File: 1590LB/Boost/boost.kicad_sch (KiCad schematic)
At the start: 22 parts, among them Q201 MMBF5103, Q202 BC847C, Q203 BC857C, Q204 NMB2227A, Q205 DMMT5401, Q206 DMMT5551, Q207 DMMT5401, Q208 DMMT5401

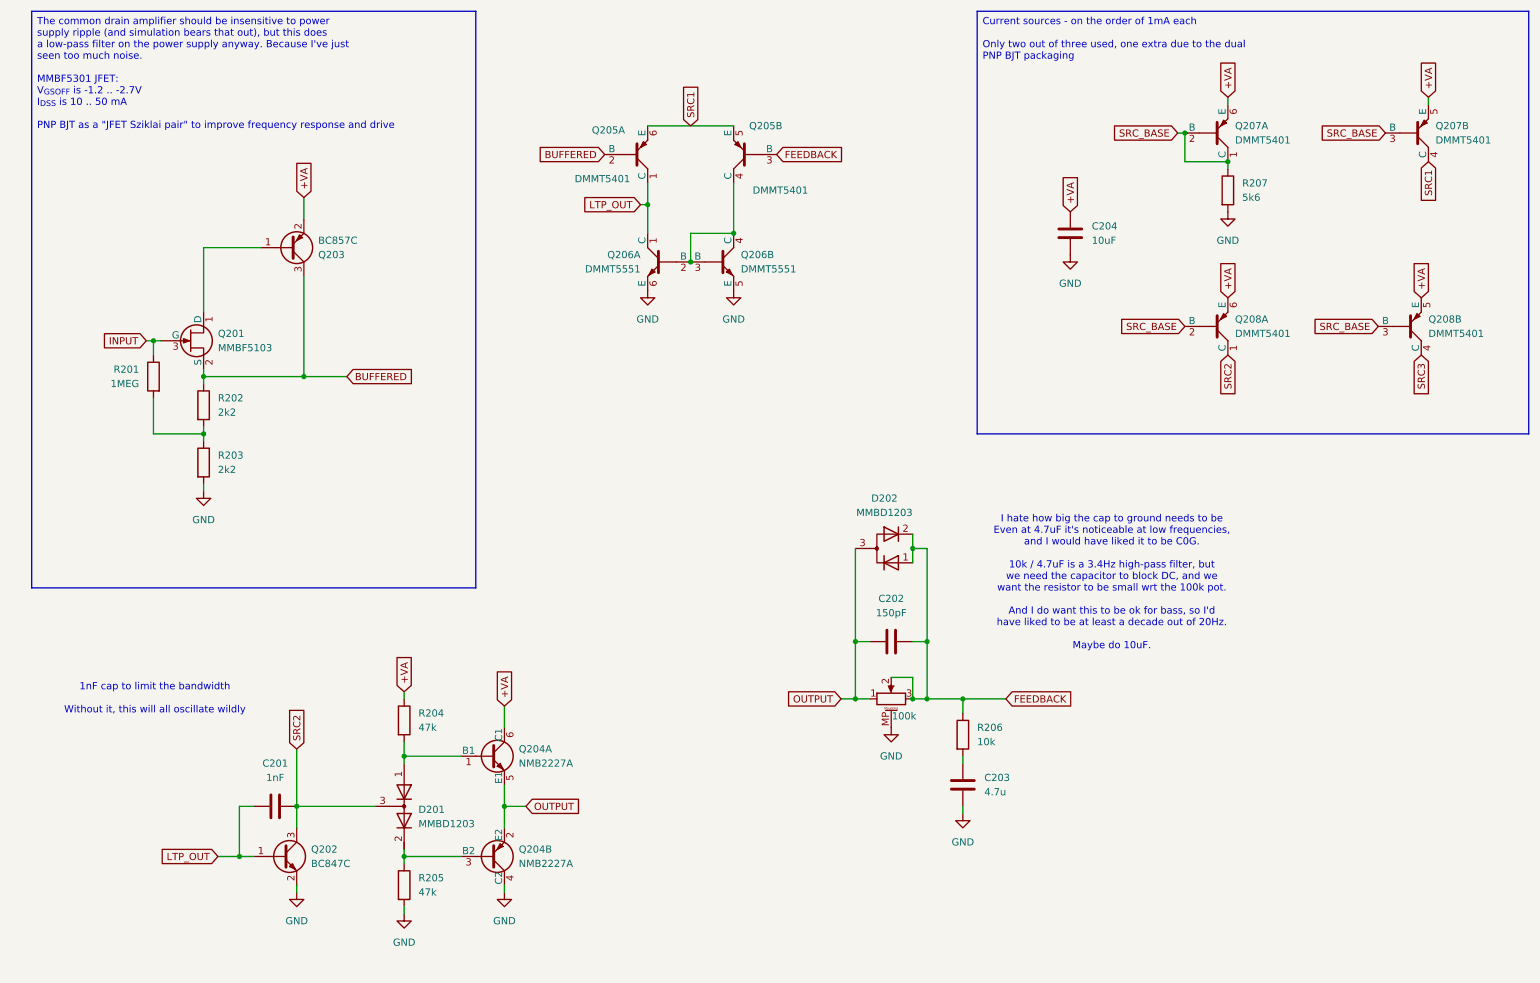
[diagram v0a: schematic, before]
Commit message: Alternate boost circuit layout
I'm not sure this fits vertically in a 1590LB, but the "everything on
top" model means that the audio jacks are very high up.  Which is not
great from a hole drilling standpoint.

So try putting the audio and DC power jacks on the back of the board,
moving the surface-mount components to the front.

And to make things fit - and because I feel like having done an op-amp
using discrete components - go back to just using an actual op-amp now.

Signed-off-by: Linus Torvalds <torvalds@linux-foundation.org>
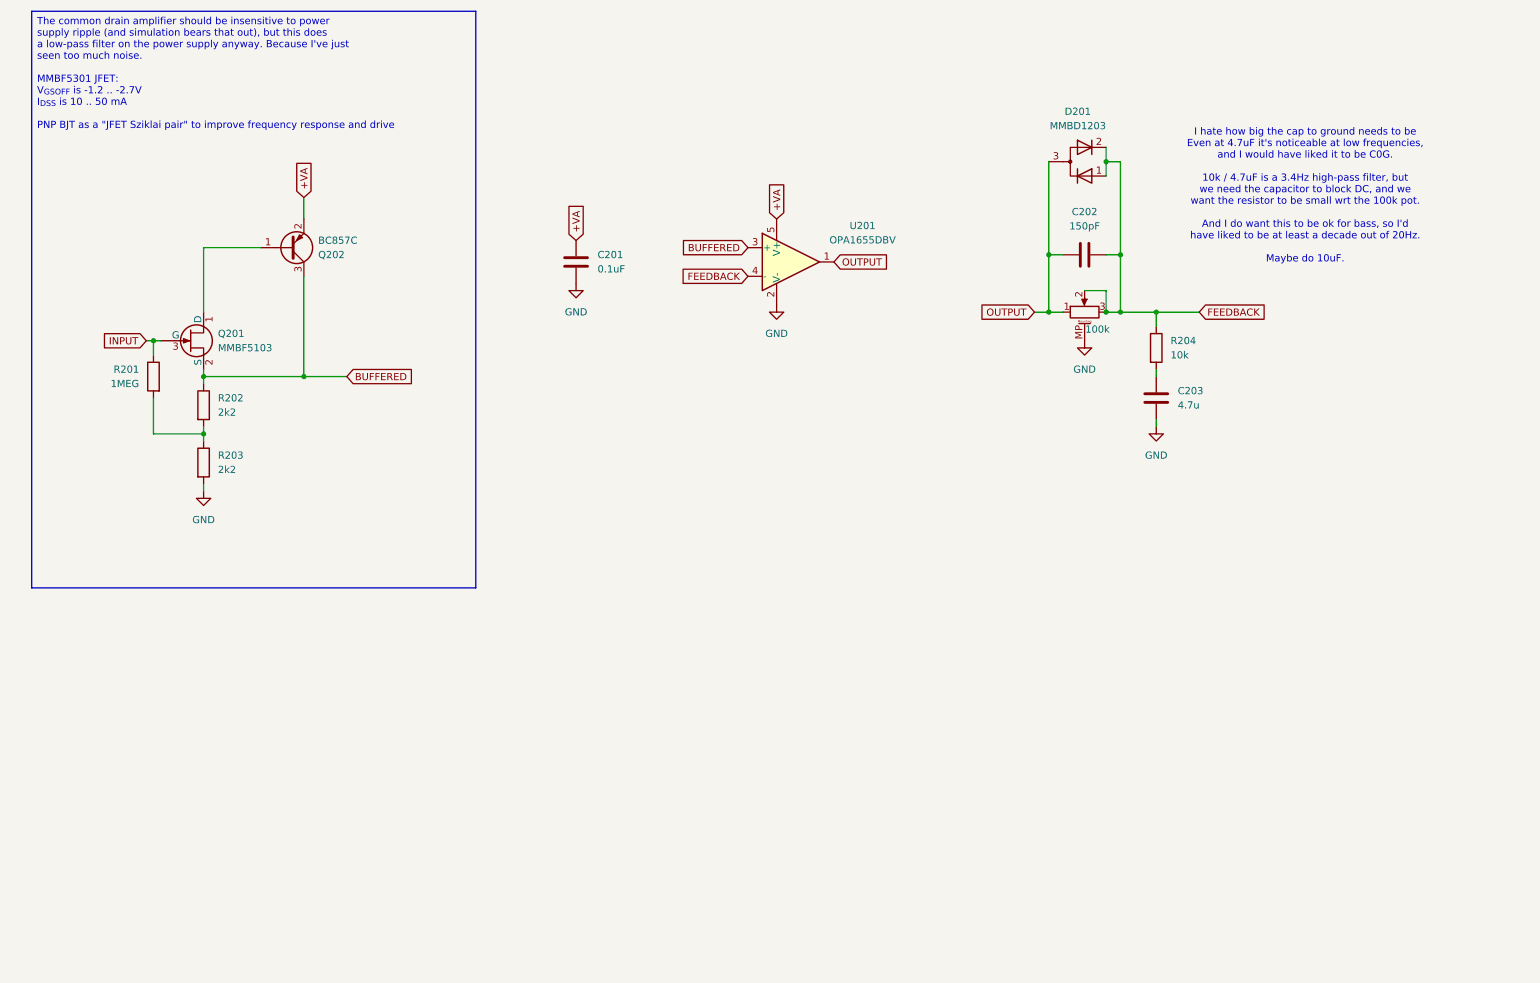
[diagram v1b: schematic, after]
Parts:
- removed C204: 10uF, Capacitor_SMD:C_1206_3216Metric, symbol Device:C
- removed D201: MMBD1203, Package_TO_SOT_SMD:SOT-23, symbol Device:D_Dual_Series_AKC
- removed Q202: BC847C, Package_TO_SOT_SMD:SOT-23, symbol Mylib:BC847C
- removed Q204: NMB2227A, Package_SO:TSOP-6_1.65x3.05mm_P0.95mm, symbol Mylib:NMB2227A
- removed Q205, Q207, Q208: DMMT5401, Package_TO_SOT_SMD:SOT-23-6, symbol Mylib:DMMT5401
- removed Q206: DMMT5551, Package_TO_SOT_SMD:SOT-23-6, symbol Mylib:DMMT5551
- removed R204, R205: 47k, Resistor_SMD:R_0805_2012Metric, symbol Device:R
- removed R207: 5k6, Resistor_SMD:R_0805_2012Metric, symbol Device:R
- added U201: OPA1655DBV, Package_TO_SOT_SMD:SOT-23-5, symbol Amplifier_Operational:OPA1655DBV
- C201: value 1nF -> 0.1uF; footprint Capacitor_SMD:C_1206_3216Metric -> Mylib:C_0704_1810Metric
- renumbered D202 to D201, Q203 to Q202, R206 to R204
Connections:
- net LTP_OUT is gone; now on net +VA: C201.2
- net SRC2 is gone; now on net GND: C201.1
- net +VA: now also U201.5 (V+)
- net BUFFERED: now also U201.3 (+)
- net FEEDBACK: now also U201.4 (-)
- net GND: now also U201.2 (V-)
- net OUTPUT: now also U201.1
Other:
- note removed: "1nF cap to limit the bandwidth Without it, this will all oscillate wildly"
- moved on the sheet: C202, C203, D201, R204

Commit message: Make the boost circuit a bit more interesting
The clean boost with some clipping was very boring, both from a sound
and a circuit standpoint.

This one isn't any better from a sound standpoint, but at least it's a
bit more interesting.  Instead of a boost pot and clipping diodes, this
has a pot that affects the biasing of the input JFET, and a fixed 10x
voltage boost with a final volume pot.

End result: it also clips, but the clipping is based on how badly the
input transistor is biased, so now you have a bit more control over the
result.

Useful? No.  But I'm back to using discrete components, because the
whole op-amp thing was just too boring.  If I want to use pre-made
circuits, I can do that on the MCU board, let's keep the analog boards
discrete.

That said, I've made the resistors and capacitors small, because I'll
just use this one for the JLCPCB assembly testing.  I did send off a
copy of the MCU board too, which is probably completely stupid - the
first PCBA board I do shouldn't have been that complex.  But maybe it
works (after I figure out the programming - even if the board is fine,
I'll have to do the SW side too to even test it).

Anyway, this one I can have assembled - and test - without then having
to write any code for various i2s things that I have no idea about.

Oh, and I still call this a "1590LB" boost board, even though I actually
ended up deciding that I'll just 3D-print the enclosure.  So it's not
really a 1590LB, it's a 45x50mm board that I'll just print a custom
enclosure for.  I actually really liked how one of my test enclosures
ended up looking, and not being limited to standard aluminum boxes is
liberating.

Signed-off-by: Linus Torvalds <torvalds@linux-foundation.org>
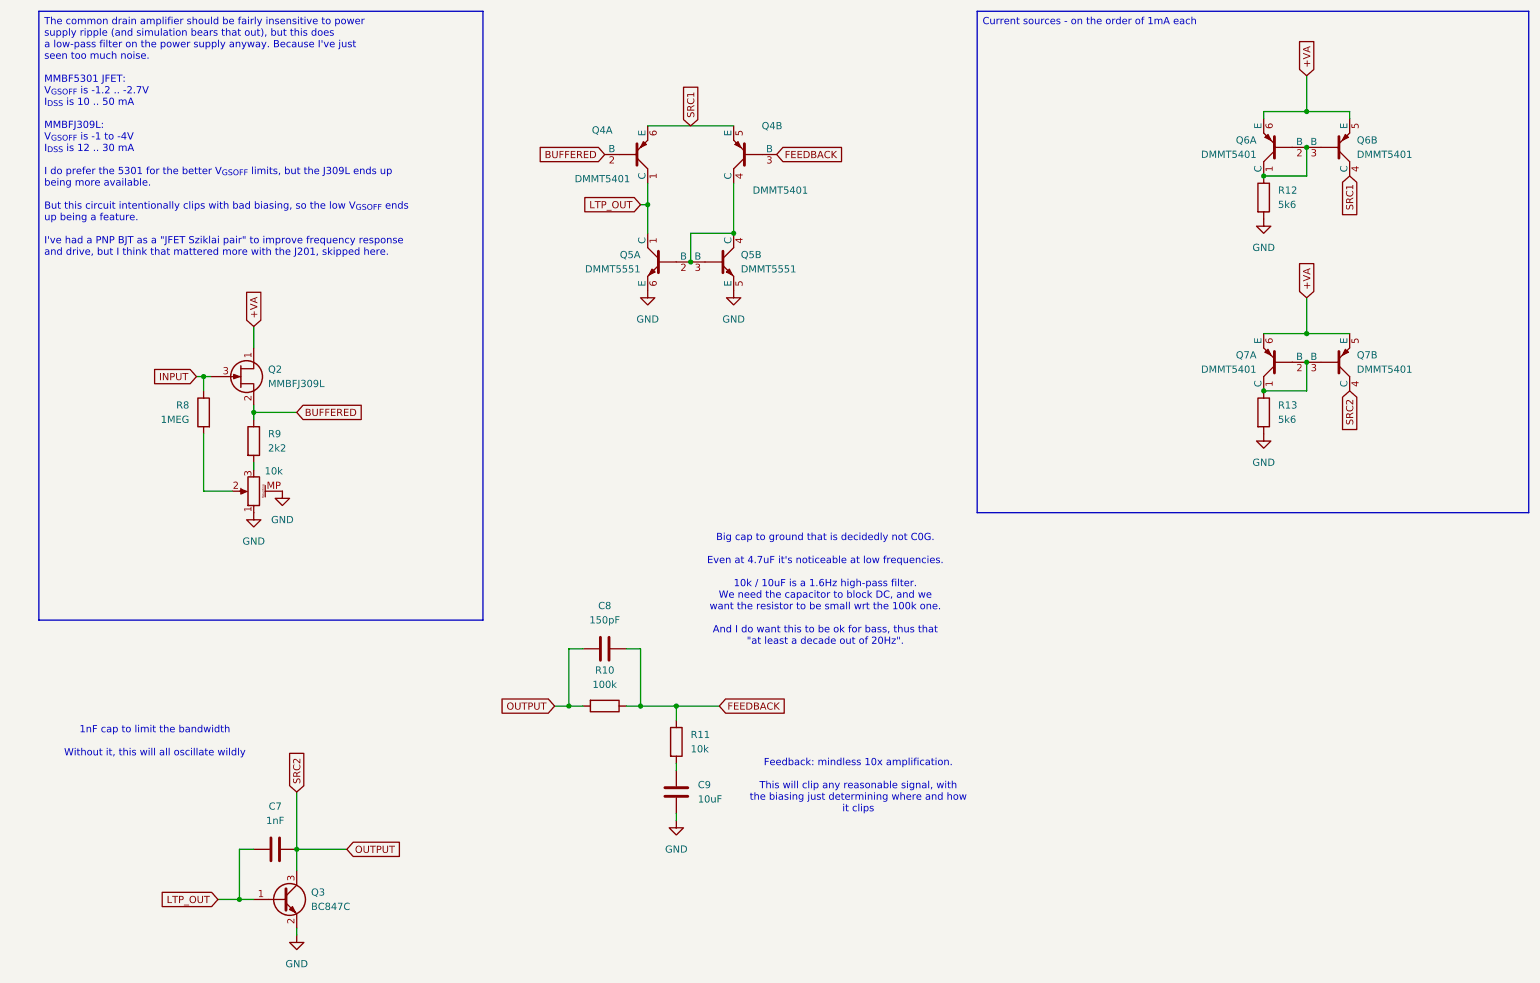
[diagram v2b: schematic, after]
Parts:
- removed C201: 0.1uF, Mylib:C_0704_1810Metric, symbol Device:C
- removed D201: MMBD1203, Package_TO_SOT_SMD:SOT-23, symbol Device:D_Dual_Series_AKC_Parallel
- removed Q201: MMBF5103, Package_TO_SOT_SMD:SOT-23, symbol Mylib:MMBF5103
- removed Q202: BC857C, Package_TO_SOT_SMD:SOT-23, symbol Mylib:BC857C
- removed R202: 2k2, Resistor_SMD:R_0805_2012Metric, symbol Device:R
- removed RV201: 100k, Mylib:Potentiometer_9mm_MP, symbol Device:R_Potentiometer_MountingPin
- removed U201: OPA1655DBV, Package_TO_SOT_SMD:SOT-23-5, symbol Amplifier_Operational:OPA1655DBV
- added C7: 1nF, Capacitor_SMD:C_0402_1005Metric, symbol Device:C
- added Q2: MMBFJ309L, Package_TO_SOT_SMD:SOT-23, symbol Device:Q_NJFET_DSG
- added Q3: BC847C, Package_TO_SOT_SMD:SOT-23, symbol Mylib:BC847C
- added Q4, Q6, Q7: DMMT5401, Package_TO_SOT_SMD:SOT-23-6, symbol Mylib:DMMT5401
- added Q5: DMMT5551, Package_TO_SOT_SMD:SOT-23-6, symbol Mylib:DMMT5551
- added R10: 100k, Resistor_SMD:R_0402_1005Metric, symbol Device:R
- added R12, R13: 5k6, Resistor_SMD:R_0402_1005Metric, symbol Device:R
- added RV2: 10k, Mylib:Potentiometer_9mm_MP, symbol Device:R_Potentiometer_MountingPin
- C8: renamed from C202; footprint Capacitor_SMD:C_1206_3216Metric -> Capacitor_SMD:C_0402_1005Metric
- C9: renamed from C203; value 4.7u -> 10uF; footprint Capacitor_SMD:C_1206_3216Metric -> Capacitor_SMD:C_0603_1608Metric
- R11: renamed from R204; footprint Resistor_SMD:R_0805_2012Metric -> Resistor_SMD:R_0402_1005Metric
- R8: renamed from R201; footprint Resistor_SMD:R_0805_2012Metric -> Resistor_SMD:R_0402_1005Metric
- R9: renamed from R203; footprint Resistor_SMD:R_0805_2012Metric -> Resistor_SMD:R_0402_1005Metric
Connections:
- net +VA: now also Q2.1 (D), Q6.5 (E), Q6.6 (E), Q7.5 (E), Q7.6 (E)
- net BUFFERED: now also R9.1, Q2.2 (S), Q4.2 (B)
- net FEEDBACK: now also Q4.3 (B), R10.1
- net GND: now also Q3.2 (E), Q5.5 (E), Q5.6 (E), R12.2, R13.2, RV2.1, RV2.MP (MountPin); no longer R9.2
- net INPUT: now also Q2.3 (G)
- net OUTPUT: now also C7.1, Q3.3 (C), Q7.4 (C), R10.2
- net at R8.2: now also RV2.2; no longer R9.1
- new net: Q4.4 (C), Q5.2 (B), Q5.3 (B), Q5.4 (C)
- new net: Q7.1 (C), Q7.2 (B), Q7.3 (B), R13.1
- new net: R9.2, RV2.3
- new net: Q6.1 (C), Q6.2 (B), Q6.3 (B), R12.1
- new net LTP_OUT: C7.2, Q3.1 (B), Q4.1 (C), Q5.1 (C)
- new net SRC1: Q4.5 (E), Q4.6 (E), Q6.4 (C)
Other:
- note added: "1nF cap to limit the bandwidth Without it, this will all oscillate wildly"
- note added: "Big cap to ground that is decidedly not C0G. Even at 4.7uF it's noticeable at low frequencies. 10k / 10uF is a 1.6Hz high-pass filter. We need the capacitor to block DC, and we want the resistor to be small wrt the 100k one. And I do want this to be ok for bass, thus that "at least a decade out of 20Hz"."
- note added: "Feedback: mindless 10x amplification. This will clip any reasonable signal, with the biasing just determining where and how it clips"
- note removed: "I hate how big the cap to ground needs to be Even at 4.7uF it's noticeable at low frequencies, and I would have liked it to be C0G. 10k / 4.7uF is a 3.4Hz high-pass filter, but we need the capacitor to block DC, and we want the resistor to be small wrt the 100k pot. And I do want this to be ok for bass, so I'd have liked to be at least a decade out of 20Hz. Maybe do 10uF."
- moved on the sheet: C8, C9, R11, R8, R9

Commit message: 1590LB boost / dirt circuit: add LCSC parts numbers
The PMV250 PNP high-side MOSFET is now a AO3401A, and the BC847C is now
a BC849C instead.  Because those were what I went with at JLCPCB.

It's kind of stupid to have this assembled by machine, since it would be
easy to do by hand (admittedly with slightly different size choices),
and this is not a particularly good design for JLCPCB anyway since all
those matched dual transistors are extended parts etc.

But the point was mainly to do PCBA with a simple board so that I can
actually verify that I did it right.  When the RP2354A comes back, it
will take some coding to get it to do anything at all, so if I screwed
up the hw, it's not going to be as obvious (unless I did it really badly
and the magic smoke escapes).

With this, it's going to be pretty obvious when it doesn't work that my
hw design is just wrong.  Or maybe it works fine - it _should_.  I've
successfully tested a very similar basic circuit, but this does have a
different JFET and some other changes.

Anyway, it's sent off.  When I get back home from travels, I should have
something to test.

Signed-off-by: Linus Torvalds <torvalds@linux-foundation.org>
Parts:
- C7: LCSC PN (none) -> C1523
- C8: LCSC PN (none) -> C710836
- C9: LCSC PN (none) -> C91606
- Q2: LCSC PN (none) -> C58012
- Q3: value BC847C -> BC849C; LCSC PN (none) -> C334244
- Q4, Q6, Q7: LCSC PN (none) -> C154733
- Q5: LCSC PN (none) -> C445514
- R10: LCSC PN (none) -> C25741
- R11: LCSC PN (none) -> C25744
- R12, R13: value 5k6 -> 5k1; LCSC PN (none) -> C25905
- R8: LCSC PN (none) -> C26083
- R9: LCSC PN (none) -> C25879
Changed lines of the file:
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@@
 			)
 		)
+		(property "LCSC PN" "C710836"
+			(at 115.57 127 90)
+			(effects
+				(font
+					(size 1.27 1.27)
+				)
+				(hide yes)
+			)
+		)
 		(pin "2"
 		)
@@
 			)
 		)
+		(property "LCSC PN" "C154733"
+			(at 139.7 39.37 0)
+			(effects
+				(font
+					(size 1.27 1.27)
+				)
+				(hide yes)
+			)
+		)
 		(pin "6"
 		)
@@
 			)
 		)
+		(property "LCSC PN" "C154733"
+			(at 233.68 76.2 0)
+			(effects
+				(font
+					(size 1.27 1.27)
+				)
+				(hide yes)
+			)
+		)
 		(pin "1"
 		)
@@
 			)
 		)
+		(property "LCSC PN" "C58012"
+			(at 50.8 78.74 0)
+			(effects
+				(font
+					(size 1.27 1.27)
+				)
+				(hide yes)
+			)
+		)
 		(pin "1"
 		)
@@
 			)
 		)
+		(property "LCSC PN" ""
+			(at 53.34 99.06 0)
+			(effects
+				(font
+					(size 1.27 1.27)
+				)
+				(hide yes)
+			)
+		)
 		(pin "2"
 		)
@@
 			)
 		)
+		(property "LCSC PN" "C154733"
+			(at 246.38 76.2 0)
+			(effects
+				(font
+					(size 1.27 1.27)
+				)
+				(hide yes)
+			)
+		)
 		(pin "1"
 		)
@@
 			)
 		)
+		(property "LCSC PN" "C25741"
+			(at 115.57 137.16 90)
+			(effects
+				(font
+					(size 1.27 1.27)
+				)
+				(hide yes)
+			)
+		)
 		(pin "1"
 		)
@@
 			)
 		)
-		(property "Value" "BC847C"
+		(property "Value" "BC849C"
 			(at 63.5 172.7199 0)
 			(effects
@@
 			)
 		)
-		(property "Sim.Library" "spice/BC847C.lib"
+		(property "Sim.Library" "spice/BC849C.lib"
 			(at 58.42 186.69 0)
 			(effects
@@
 			)
 		)
-		(property "Sim.Name" "BC847C"
+		(property "Sim.Name" "BC849C"
 			(at 59.69 189.23 0)
 			(effects
@@
 			)
 		)
-		(property "Sim.Pins" "1=B 2=E 3=C"
+		(property "Sim.Pins" "1=2 2=3 3=1"
 			(at 58.42 191.77 0)
 			(effects
@@
 			)
 		)
+		(property "LCSC PN" "C334244"
+			(at 58.42 171.45 0)
+			(effects
+				(font
+					(size 1.27 1.27)
+				)
+				(hide yes)
+			)
+		)
 		(pin "2"
 		)
@@
 			)
 		)
-		(property "Value" "5k6"
+		(property "Value" "5k1"
 			(at 234.95 48.26 0)
 			(effects
@@
 			)
 		)
+		(property "LCSC PN" "C25905"
+			(at 232.41 46.99 0)
+			(effects
+				(font
+					(size 1.27 1.27)
+				)
+				(hide yes)
+			)
+		)
 		(pin "1"
 		)
@@
 			)
 		)
+		(property "LCSC PN" "C154733"
+			(at 246.38 38.1 0)
+			(effects
+				(font
+					(size 1.27 1.27)
+				)
+				(hide yes)
+			)
+		)
 		(pin "1"
 		)
@@
 			)
 		)
+		(property "LCSC PN" "C91606"
+			(at 128.27 152.4 0)
+			(effects
+				(font
+					(size 1.27 1.27)
+				)
+				(hide yes)
+			)
+		)
 		(pin "2"
 		)
@@
 			)
 		)
+		(property "LCSC PN" "C154733"
+			(at 121.92 39.37 0)
+			(effects
+				(font
+					(size 1.27 1.27)
+				)
+				(hide yes)
+			)
+		)
 		(pin "6"
 		)
@@
 			)
 		)
+		(property "LCSC PN" "C154733"
+			(at 233.68 38.1 0)
+			(effects
+				(font
+					(size 1.27 1.27)
+				)
+				(hide yes)
+			)
+		)
 		(pin "1"
 		)
@@
 			)
 		)
-		(property "Value" "5k6"
+		(property "Value" "5k1"
 			(at 234.95 86.36 0)
 			(effects
@@
 			)
 		)
+		(property "LCSC PN" "C25905"
+			(at 232.41 85.09 0)
+			(effects
+				(font
+					(size 1.27 1.27)
+				)
+				(hide yes)
+			)
+		)
 		(pin "1"
 		)
@@
 			)
 		)
+		(property "LCSC PN" "C25879"
+			(at 53.34 90.17 0)
+			(effects
+				(font
+					(size 1.27 1.27)
+				)
+				(hide yes)
+			)
+		)
 		(pin "1"
 		)
@@
 			)
 		)
+		(property "LCSC PN" "C25744"
+			(at 128.27 143.51 0)
+			(effects
+				(font
+					(size 1.27 1.27)
+				)
+				(hide yes)
+			)
+		)
 		(pin "1"
 		)
@@
 			)
 		)
+		(property "LCSC PN" "C1523"
+			(at 57.15 162.56 90)
+			(effects
+				(font
+					(size 1.27 1.27)
+				)
+				(hide yes)
+			)
+		)
 		(pin "2"
 		)
@@
 			)
 		)
+		(property "LCSC PN" "C445514"
+			(at 137.16 58.42 0)
+			(effects
+				(font
+					(size 1.27 1.27)
+				)
+				(hide yes)
+			)
+		)
 		(pin "1"
 		)
@@
 			)
 		)
+		(property "LCSC PN" "C445514"
+			(at 124.46 58.42 0)
+			(effects
+				(font
+					(size 1.27 1.27)
+				)
+				(hide yes)
+			)
+		)
 		(pin "1"
 		)
@@
 			(at 44.45 85.09 0)
 			(effects
+				(font
+					(size 1.27 1.27)
+				)
+				(hide yes)
+			)
+		)
+		(property "LCSC PN" "C26083"
+			(at 44.45 85.09 0)
+			(effects
